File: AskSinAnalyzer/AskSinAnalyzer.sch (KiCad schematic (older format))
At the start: 14 parts, among them J1 Supply, SW1 SW_DIP_x04, SW2 SW_Push, U1 ESP-WROOM-32_DEVKIT_V4, U2 Arduino_Pro_Mini, U3 CC1101, U4 TJCTM24028-SPI

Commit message: AskSinAnalyzer PCB
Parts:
- removed C1: 1u, Capacitors_SMD:C_0805_HandSoldering, symbol Device:C
- removed J1: Supply, Pin_Headers:Pin_Header_Straight_1x02_Pitch2.54mm, symbol Connector_Generic:Conn_01x02
- removed JP1: ~, Jumper:SolderJumper-2_P1.3mm_Open_RoundedPad1.0x1.5mm, symbol Jumper:SolderJumper_2_Open
- removed LED1: GREEN, LEDs:LED_D3.0mm_Horizontal_O3.81mm_Z6.0mm, symbol Device:LED
- removed LED2: YELLOW, LEDs:LED_D3.0mm_Horizontal_O3.81mm_Z6.0mm, symbol Device:LED
- removed R1, R2: 330, Resistors_SMD:R_0805_HandSoldering, symbol Device:R
- removed R3: 10k, Resistors_SMD:R_0805_HandSoldering, symbol Device:R
- removed SW1: SW_DIP_x04, Buttons_Switches_THT:SW_DIP_x4_W7.62mm_Piano, symbol Switch:SW_DIP_x04
- removed SW2: SW_Push, Buttons_Switches_THT:SW_Tactile_SPST_Angled_PTS645Vx83-2LFS, symbol Switch:SW_Push
- removed U1: ESP-WROOM-32_DEVKIT_V4, myEspModules:ESP-WROOM-32_DEVKIT_V4, symbol myEspModules:ESP-WROOM-32_DEVKIT_V4
- removed U2: Arduino_Pro_Mini, myArduinoModules:Arduino_Pro_Mini_wo_Ax, symbol myArduinoModules:Arduino_Pro_Mini
- removed U3: CC1101, CC1101_Module:CC1101_Module, symbol CC1101_Module:CC1101
- removed U4: TJCTM24028-SPI, myDisplays:TJCTM24028-SPI, symbol myDisplays:TJCTM24028-SPI
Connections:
- net labels removed: +3.3V, +5V, BUTTON1, CC_CS, CC_SCK, ESP_RX, ESP_TX, GDO0, GND, LED_AP, LED_RX, MISO, MOSI, SD_CS, SD_TFT_MISO, SD_TFT_MOSI, SD_TFT_SCK, SW_DETAIL, SW_LINES, SW_ONLINE, SW_UNUSED, TFT_CS, TFT_DC, TFT_LED, TFT_RESET, T_CS, T_IRQ
- wire segments 101 -> 2
- no-connect marks 36 -> 0

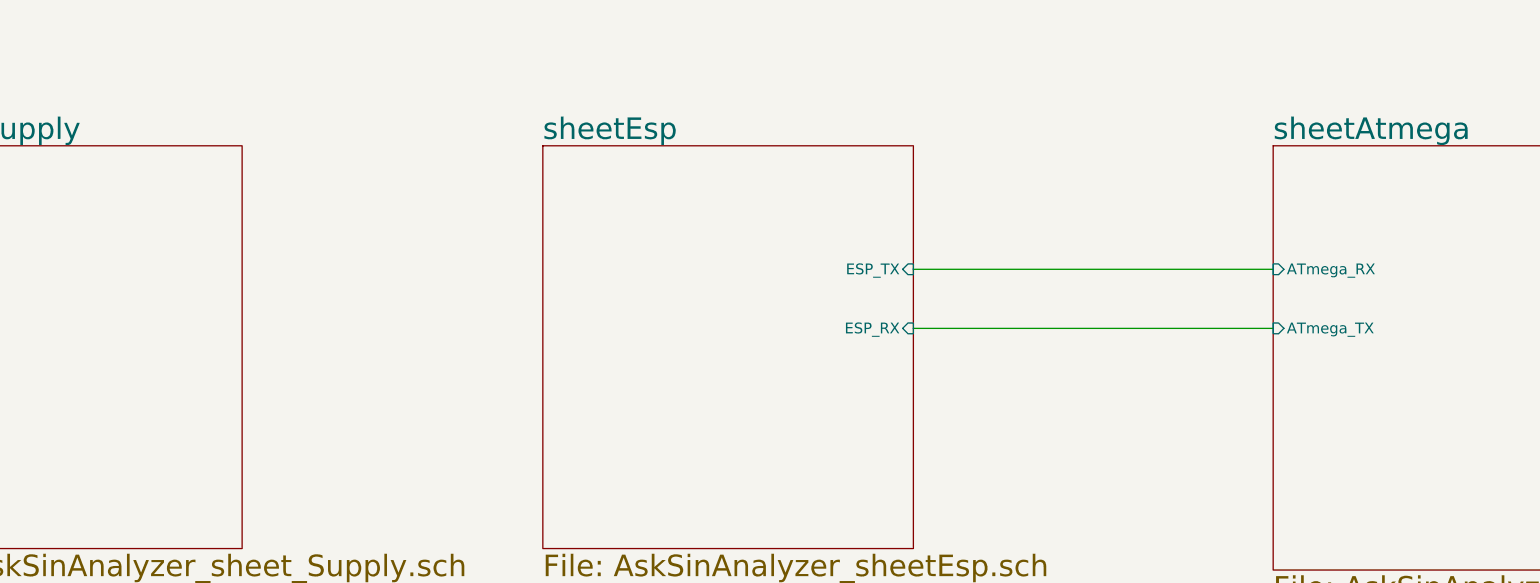
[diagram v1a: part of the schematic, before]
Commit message: AskSinAnalyzer PCB V2.0 RC1
added a FTDI FT245 to flash and debug ESP32
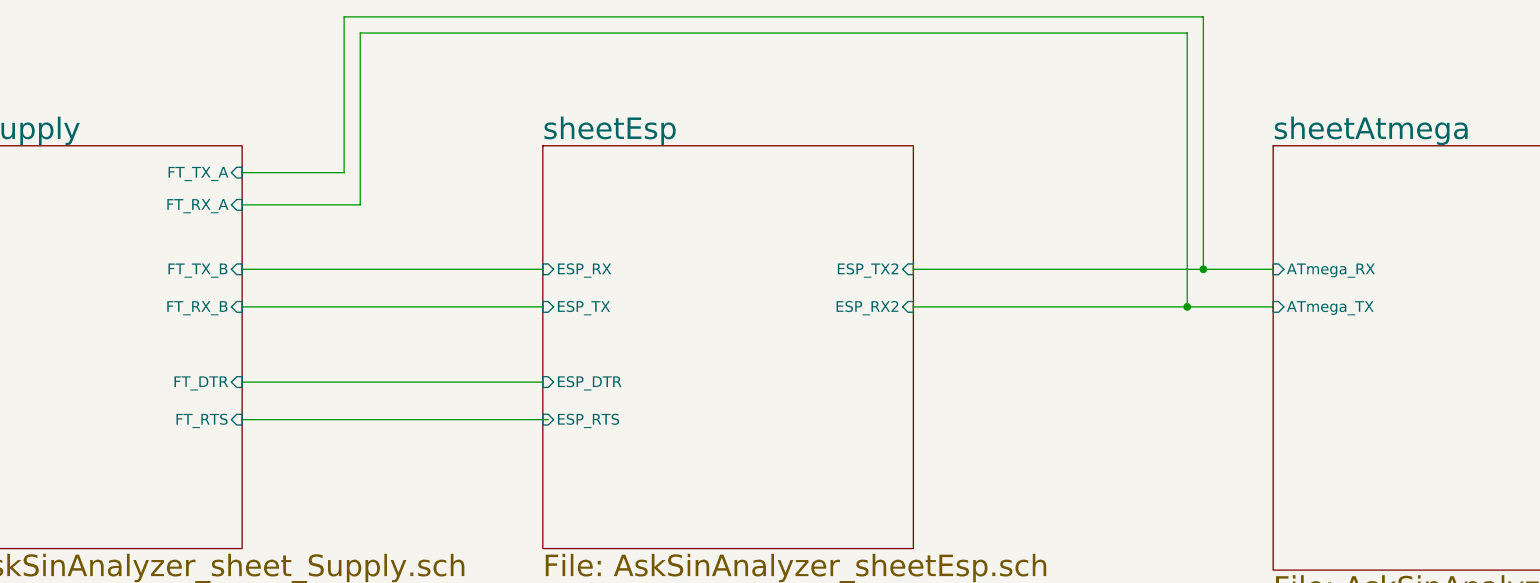
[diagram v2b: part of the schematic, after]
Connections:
- wire segments 2 -> 16
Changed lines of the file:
@@
 Title "AskSin Analyzer"
 Date "2019-07-07"
-Rev "0.1"
+Rev "2.0 RC1"
 Comp "stan23 CC BY-NC-SA"
 Comment1 ""
@@
 F0 "sheetEsp" 100
 F1 "AskSinAnalyzer_sheetEsp.sch" 100
-F2 "ESP_RX" I R 5700 4000 50
-F3 "ESP_TX" I R 5700 3725 50
+F2 "ESP_RTS" I L 3975 4425 50
+F3 "ESP_DTR" I L 3975 4250 50
+F4 "ESP_RX2" I R 5700 3900 50
+F5 "ESP_TX2" I R 5700 3725 50
+F6 "ESP_RX" I L 3975 3725 50
+F7 "ESP_TX" I L 3975 3900 50
 $EndSheet
 $Sheet
@@
 F1 "AskSinAnalyzer_sheetAtmega.sch" 100
 F2 "ATmega_RX" I L 7375 3725 50
-F3 "ATmega_TX" I L 7375 4000 50
+F3 "ATmega_TX" I L 7375 3900 50
 $EndSheet
 Wire Wire Line
-	5700 3725 7375 3725
-Wire Wire Line
-	7375 4000 5700 4000
+	5700 3725 7050 3725
 $Sheet
 S 975  3150 1600 1875
@@
 F0 "sheetSupply" 100
 F1 "AskSinAnalyzer_sheet_Supply.sch" 100
+F2 "FT_RTS" I R 2575 4425 50
+F3 "FT_DTR" I R 2575 4250 50
+F4 "FT_TX_A" I R 2575 3275 50
+F5 "FT_TX_B" I R 2575 3725 50
+F6 "FT_RX_A" I R 2575 3425 50
+F7 "FT_RX_B" I R 2575 3900 50
 $EndSheet
+Wire Wire Line
+	2575 4425 4000 4425
+Wire Wire Line
+	3975 3725 2575 3725
+Wire Wire Line
+	2575 3275 3050 3275
+Wire Wire Line
+	3050 3275 3050 2550
+Wire Wire Line
+	3050 2550 7050 2550
+Wire Wire Line
+	7050 2550 7050 3725
+Connection ~ 7050 3725
+Wire Wire Line
+	7050 3725 7375 3725
+Wire Wire Line
+	3125 2625 6975 2625
+Wire Wire Line
+	6975 2625 6975 3900
+Wire Wire Line
+	3975 3900 2575 3900
+Wire Wire Line
+	2575 3425 3125 3425
+Wire Wire Line
+	3125 3425 3125 2625
+Wire Wire Line
+	7375 3900 6975 3900
+Connection ~ 6975 3900
+Wire Wire Line
+	6975 3900 5700 3900
+Wire Wire Line
+	2575 4250 3975 4250
 $EndSCHEMATC

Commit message: AskSinAnalyzer PCB V2.0
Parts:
- added JP1, JP2: ~, Jumper:SolderJumper-2_P1.3mm_Open_RoundedPad1.0x1.5mm, symbol Jumper:SolderJumper_2_Open
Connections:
- wire segments 16 -> 18
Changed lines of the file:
@@
 F0 "sheetEsp" 100
 F1 "AskSinAnalyzer_sheetEsp.sch" 100
-F2 "ESP_RTS" I L 3975 4425 50
-F3 "ESP_DTR" I L 3975 4250 50
-F4 "ESP_RX2" I R 5700 3900 50
-F5 "ESP_TX2" I R 5700 3725 50
-F6 "ESP_RX" I L 3975 3725 50
-F7 "ESP_TX" I L 3975 3900 50
+F2 "ESP_DTR" I L 3975 4250 50
+F3 "ESP_RX2" I R 5700 3900 50
+F4 "ESP_TX2" I R 5700 3725 50
+F5 "ESP_RX" I L 3975 3725 50
+F6 "ESP_TX" I L 3975 3900 50
+F7 "ESP_RTS" I L 3975 4450 50
 $EndSheet
 $Sheet
@@
 $EndSheet
 Wire Wire Line
-	5700 3725 7050 3725
+	5700 3725 6400 3725
 $Sheet
 S 975  3150 1600 1875
@@
 F0 "sheetSupply" 100
 F1 "AskSinAnalyzer_sheet_Supply.sch" 100
-F2 "FT_RTS" I R 2575 4425 50
-F3 "FT_DTR" I R 2575 4250 50
-F4 "FT_TX_A" I R 2575 3275 50
-F5 "FT_TX_B" I R 2575 3725 50
-F6 "FT_RX_A" I R 2575 3425 50
-F7 "FT_RX_B" I R 2575 3900 50
+F2 "FT_DTR" I R 2575 4250 50
+F3 "FT_TX_A" I R 2575 3275 50
+F4 "FT_TX_B" I R 2575 3725 50
+F5 "FT_RX_A" I R 2575 3425 50
+F6 "FT_RX_B" I R 2575 3900 50
+F7 "FT_RTS" I R 2575 4450 50
 $EndSheet
-Wire Wire Line
-	2575 4425 4000 4425
 Wire Wire Line
 	3975 3725 2575 3725
@@
 Wire Wire Line
 	7375 3900 6975 3900
-Connection ~ 6975 3900
-Wire Wire Line
-	6975 3900 5700 3900
 Wire Wire Line
 	2575 4250 3975 4250
+Wire Wire Line
+	2575 4450 3975 4450
+$Comp
+L Jumper:SolderJumper_2_Open JP1
+U 1 1 5D7A89F0
+P 6550 3725
+F 0 "JP1" H 6550 3838 50  0000 C CNN
+F 1 "~" H 6550 3839 50  0000 C CNN
+F 2 "Jumper:SolderJumper-2_P1.3mm_Open_RoundedPad1.0x1.5mm" H 6550 3725 50  0001 C CNN
+F 3 "~" H 6550 3725 50  0001 C CNN
+	1    6550 3725
+	1    0    0    -1
+$EndComp
+Wire Wire Line
+	6700 3725 7050 3725
+$Comp
+L Jumper:SolderJumper_2_Open JP2
+U 1 1 5D7B24A6
+P 6550 3900
+F 0 "JP2" H 6550 3775 50  0000 C CNN
+F 1 "~" H 6550 4014 50  0000 C CNN
+F 2 "Jumper:SolderJumper-2_P1.3mm_Open_RoundedPad1.0x1.5mm" H 6550 3900 50  0001 C CNN
+F 3 "~" H 6550 3900 50  0001 C CNN
+	1    6550 3900
+	1    0    0    -1
+$EndComp
+Wire Wire Line
+	6400 3900 5700 3900
+Wire Wire Line
+	6700 3900 6975 3900
+Connection ~ 6975 3900
 $EndSCHEMATC

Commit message: add production data to AskSinAnalyzer PCB
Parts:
- JP1, JP2: LCSC (none) -> -
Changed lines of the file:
@@
 F 2 "Jumper:SolderJumper-2_P1.3mm_Open_RoundedPad1.0x1.5mm" H 6550 3725 50  0001 C CNN
 F 3 "~" H 6550 3725 50  0001 C CNN
+F 4 "-" H 6550 3725 50  0001 C CNN "LCSC"
 	1    6550 3725
 	1    0    0    -1
@@
 F 2 "Jumper:SolderJumper-2_P1.3mm_Open_RoundedPad1.0x1.5mm" H 6550 3900 50  0001 C CNN
 F 3 "~" H 6550 3900 50  0001 C CNN
+F 4 "-" H 6550 3900 50  0001 C CNN "LCSC"
 	1    6550 3900
 	1    0    0    -1
